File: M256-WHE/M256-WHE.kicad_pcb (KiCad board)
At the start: 2 copper layers, 301.8 x 97 mm, 318 parts, among them J1 JST_SH, J2 TC2030, SW1 TS-1187A-B-A-B, SW2 TS-1187A-B-A-B, U1 USBLC6-2SC6, U2 TLV75733PDBV, U3 XC6206P332MR-G, U4 AT32F405RCT7, Y1 X322512MSB4SI

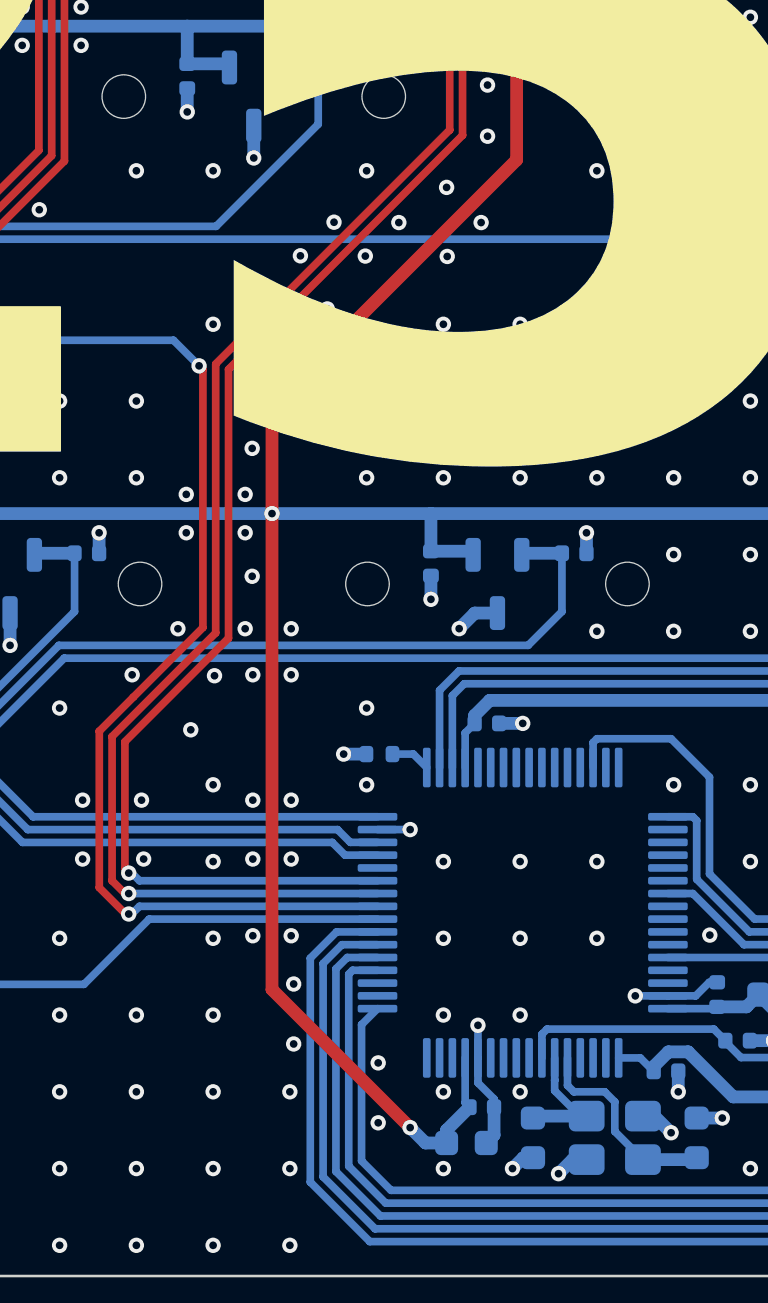
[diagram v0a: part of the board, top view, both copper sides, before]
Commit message: :art: update traces
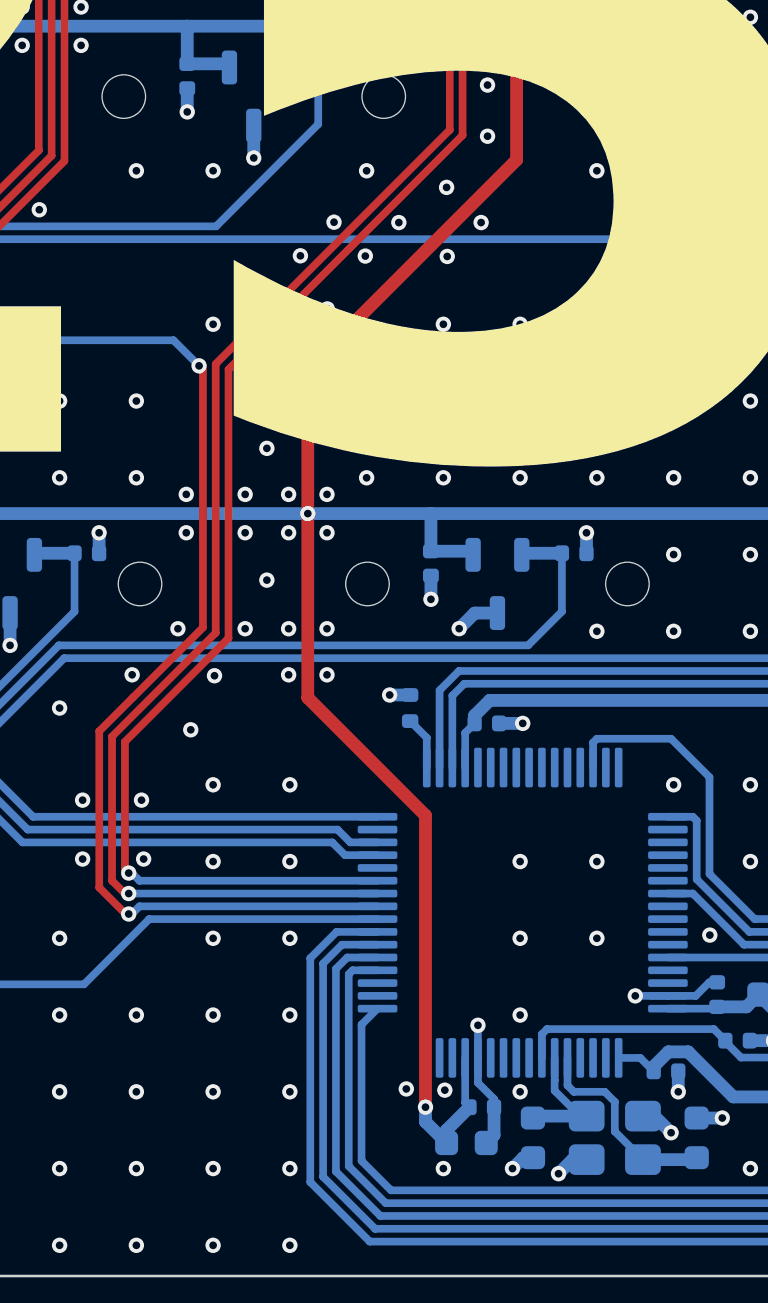
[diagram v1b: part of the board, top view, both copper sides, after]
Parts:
- moved R2 2.16 mm to (104.6, 70.0), turned to -90 degrees
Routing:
- net +3.3VA: track 1780.3 -> 1778.7 mm
- net GND: track 259.0 -> 257.6 mm, vias 2336 -> 2330
- net Net-(U4-OTGHS1_R): track 1.56 -> 2.08 mm
